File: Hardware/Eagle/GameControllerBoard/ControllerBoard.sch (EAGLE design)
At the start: 4 parts

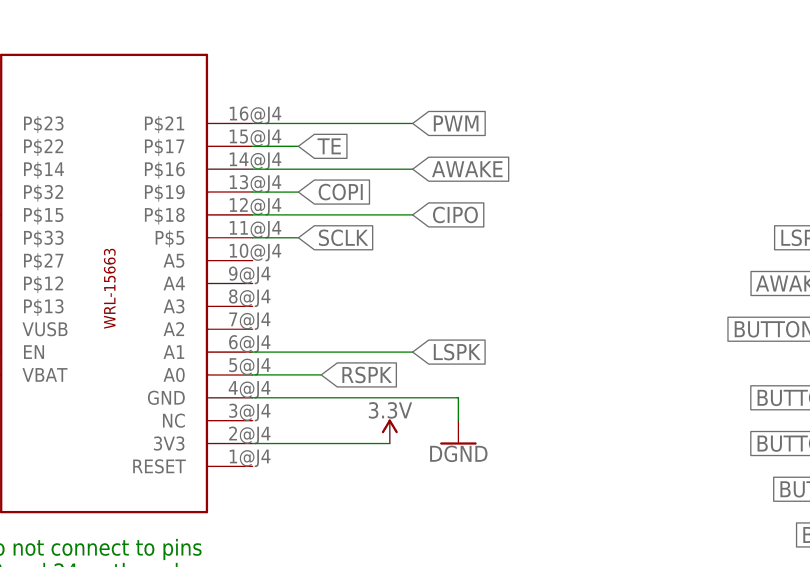
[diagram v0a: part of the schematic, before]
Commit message: Added reference for button 4 for issue #7
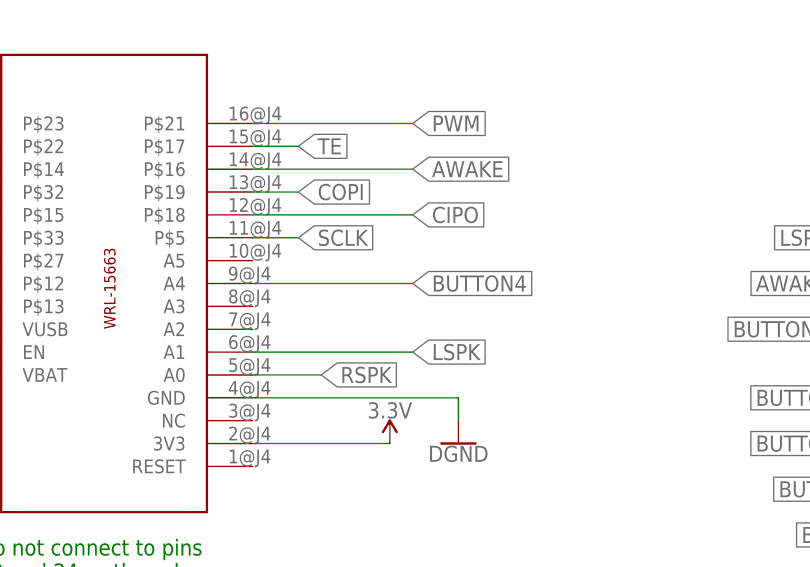
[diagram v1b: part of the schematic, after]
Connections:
- net BUTTON4: now also A1.A4
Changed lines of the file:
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@@
 <label x="167.64" y="71.12" size="1.778" layer="95" rot="R180" xref="yes" grouprefs="HEADERS"/>
+</segment>
+<segment>
+<pinref part="A1" gate="G$1" pin="A4"/>
+<wire x1="93.98" y1="99.06" x2="111.76" y2="99.06" width="0.1524" layer="91"/>
+<label x="111.76" y="99.06" size="1.778" layer="95" xref="yes"/>
 </segment>
 </net>
